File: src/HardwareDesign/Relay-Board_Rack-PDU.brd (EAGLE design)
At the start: 196 x 100 mm, 16 parts

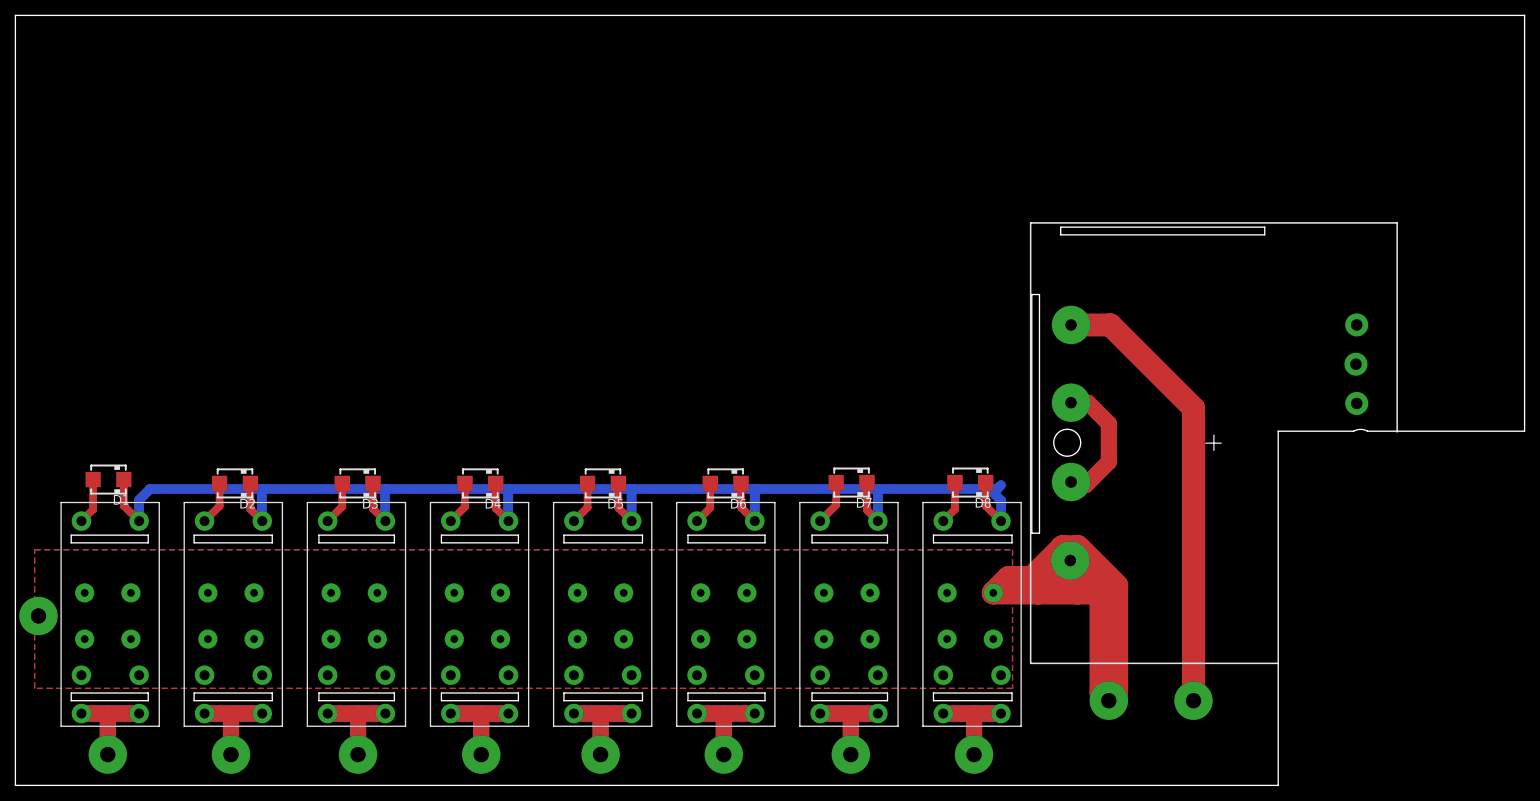
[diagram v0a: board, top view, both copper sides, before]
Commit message: add SMPS to relay board
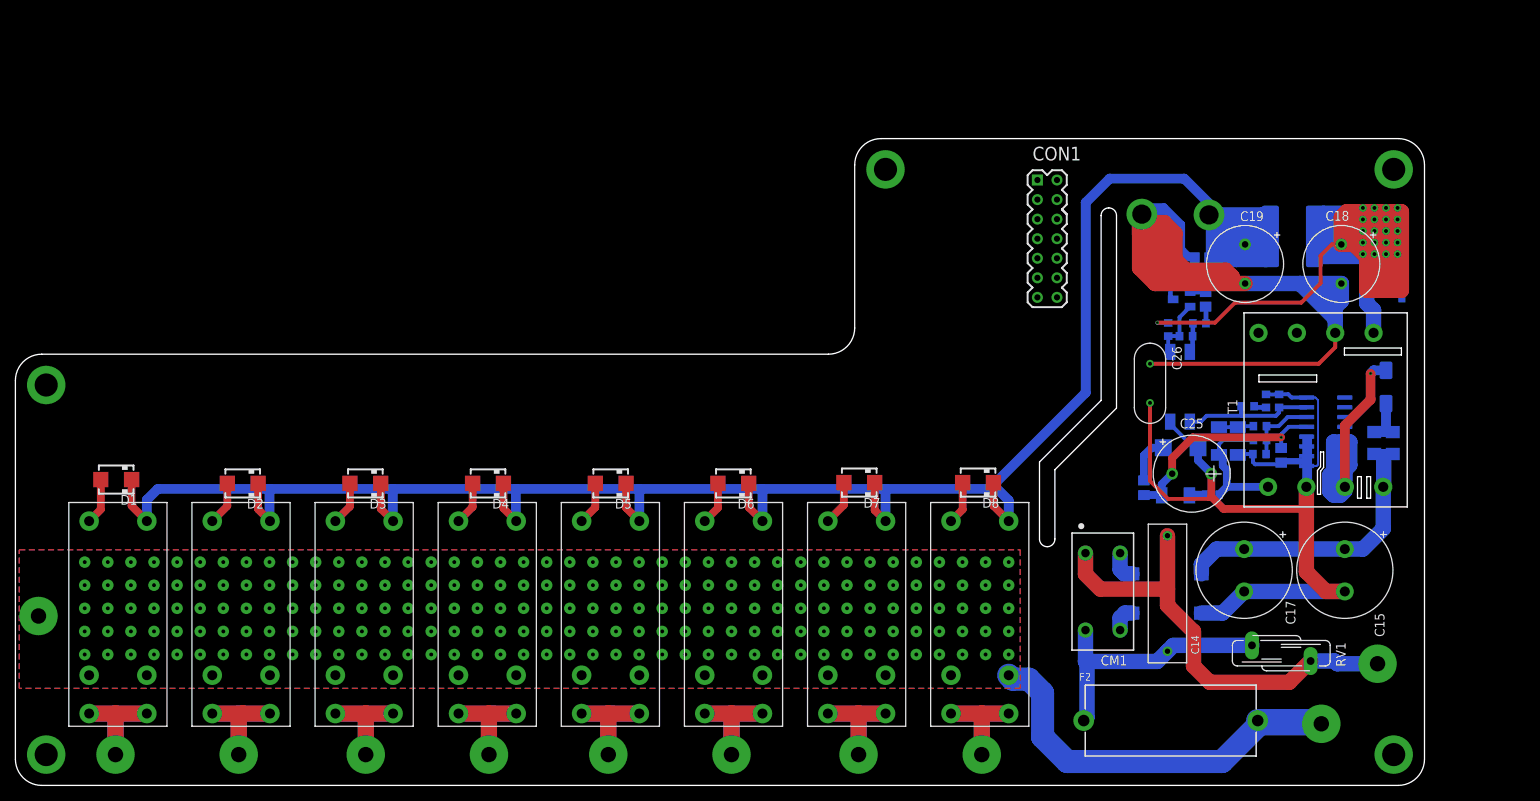
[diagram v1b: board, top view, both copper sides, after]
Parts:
- added BR1: DBLS207G, rectifier:DBS
- added C14: 100nF 275V, ds_passive:103-275V
- added C15, C17: 15uF 400V, Capacitor:CAPPRD550W110D1250H2500B
- added C16: 10nF 1kV, ds_passive:C1206
- added C18: 470uF 25V, Capacitor:CAPPRD508W65D1000H1100B
- added C19, C25: 100uF 25V, Capacitor:CAPPRD508W65D1000H1100B
- added C20: 1uF 25V, ds_passive:C0805
- added C21: 10nF 50V, ds_passive:C0805
- added C22: 2.2nF 50V, ds_passive:C0603
- added C23: 33nF 16V, ds_passive:C0603
- added C24: 220pF, ds_passive:C0805
- added C26: DE2E3KY222MA2BM01, ds_passive:AR21AC103K4R
- added CM1: 20mH CM CHOKE, ds_trafo:WE-CMB_XS_744821120
- added CON1: (no value), ds_con:2X7
- added D15: MRA4007T3G, Diodes:SMA
- added D16: STPS5H100B, ds_active:DPAK_STM
- added D17, D18, D19: BAT41ZFILM, diode:SOD-123_MINI-SMA
- added D20: MMSZ5248B-V-GS08, Diodes-2:DO214AC
- added F2: 696101000002, Wurth_Connectors_WR-FSH:696101000002
- added IC3: TS432ILT, ds_ic_vreg:SOT23
- added IC4: (no value), ds_ic_peripherals:VIPER35HD
- added L2: 3.3uH SD43-332ML, 52101-101-REV-A_v16:INDUCTOR-BOURNS_SRN8040
- added OPT2: SFH6106-2T, ds_ic_peripherals:SMD-4_SFH610X_VIS-M
- added R13: 220K 5% 0.33W 200V, ds_passive:1206
- added R14: 1K, ds_passive:0603
- added R15: 12K, ds_passive:0603
- added R16: 82K, ds_passive:0603
- added R17: 130K 1%, ds_passive:0603
- added R18: 15K 1%, ds_passive:0603
- added R19: 4.7R 1%, ds_passive:0603
- added R20: 330K 1%, ds_passive:0603
- added R21: 133K 1%, ds_passive:0603
- added R22: 30K 1%, ds_passive:0603
- added R23: 47K 1%, ds_passive:0603
- added R24: 220R, ds_passive:0805
- added RV1: B72210S0321K101, varistor:S10K40
- added T1: 750370228, ds_trafo:WE-OLSTM_EE20_L22.2W25H16
- moved D1 1.00 mm to (12.1, 39.7)
- moved D2 1.00 mm to (28.5, 39.2)
- moved D3 1.00 mm to (44.5, 39.2)
- moved D4 1.00 mm to (60.4, 39.2)
- moved D5 1.00 mm to (76.3, 39.2)
- moved D6 1.00 mm to (92.2, 39.2)
- moved D7 1.00 mm to (108.6, 39.3)
- moved D8 1.00 mm to (124.0, 39.3)
- moved REL1 1.00 mm to (12.3, 21.6)
- moved REL2 1.00 mm to (28.2, 21.6)
- moved REL3 1.00 mm to (44.2, 21.6)
- moved REL4 1.00 mm to (60.2, 21.6)
- moved REL5 1.00 mm to (76.2, 21.6)
- moved REL6 1.00 mm to (92.2, 21.6)
- moved REL7 1.00 mm to (108.2, 21.6)
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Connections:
- new net AC_LINE2: C14.2, CM1.1, RV1.2
- new net AGND: BR1.-, C15.2, C17.2, C22.2, C24.2, C25.2, C26.1, D17.A, D20.A, IC4.1, IC4.2, IC4.3, IC4.4, IC4.8, OPT2.4, R22.2, R23.2, T1.3
- new net DC_RAW: BR1.+, C15.1, C16.1, C17.1, R13.2, T1.6
- new net FB: C22.1, C23.1, IC4.7, OPT2.3
- new net GND: C18.2, C19.2, C20.2, C26.2, IC3.3, R18.2, T1.10
- new net N$12: BR1.AC2, CM1.3
- new net N$20: C14.1, CM1.2, F2.2, RV1.1
- new net N$22: C16.2, D15.C, R13.1
- new net N$23: D15.A, IC4.13, IC4.14, IC4.15, IC4.16, T1.4
- new net N$24: D16.2, T1.8
- new net N$25: C18.1, D16.3, L2.1, R14.1
- new net N$26: IC3.2, OPT2.1, R14.2, R15.1
- new net N$27: OPT2.2, R15.2, R16.1
- new net N$28: C21.1, R16.2
- new net N$29: C21.2, IC3.1, R17.2, R18.1
- new net N$30: C24.1, C25.1, D19.C, IC4.5, R24.1
- new net N$31: D19.A, R19.2
- new net N$32: D18.A, R19.1, R20.1, T1.1
- new net N$33: D17.C, D18.C, R21.1
- new net N$34: IC4.6, R20.2, R21.2, R22.1
- new net N$35: C23.2, R23.1
- new net N$36: D20.C, R24.2
- new net N$5: BR1.AC1, CM1.4
- net +12V: now also C19.1, C20.1, L2.2, R17.1
- net AC_LINE: now also F2.1
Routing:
- net GND: track 0.00 -> 193.6 mm, vias 0 -> 1
- net N$25: track 0.00 -> 164.8 mm, vias 0 -> 21
- net AGND: track 0.00 -> 118.3 mm
- net +12V: track 190.9 -> 308.1 mm, vias 0 -> 1
- net N$23: track 0.00 -> 51.0 mm, vias 0 -> 1
- net DC_RAW: track 0.00 -> 38.9 mm
- net N$20: track 0.00 -> 34.4 mm
- net N$30: track 0.00 -> 28.5 mm, vias 0 -> 1
- net AC_LINE: track 81.6 -> 59.0 mm, vias 35 -> 207
- net AC_COM: track 17.7 -> 0.00 mm, vias 2 -> 0
- net FB: track 0.00 -> 17.6 mm
- net N$32: track 0.00 -> 17.4 mm
- net N$34: track 0.00 -> 9.36 mm
- net N$26: track 0.00 -> 8.05 mm
- net N$36: track 0.00 -> 6.18 mm
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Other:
- board size 196 x 100 mm -> 183 x 84 mm

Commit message: finish relay board design
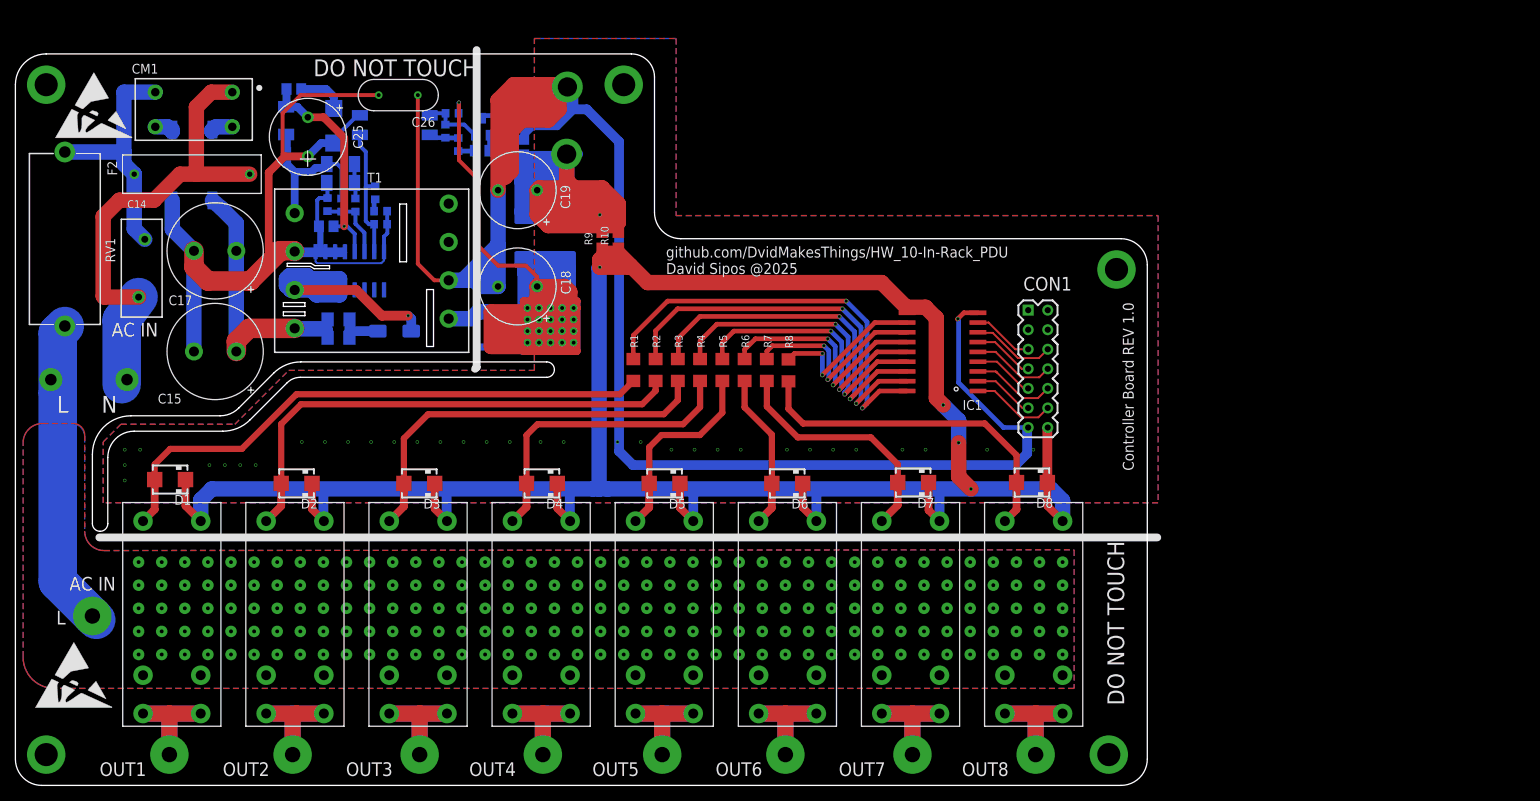
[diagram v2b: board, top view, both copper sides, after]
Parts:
- added IC1: ULN2803, ds_ic_peripherals:SO18
- added R1, R2, R3, R4, R5, R6, R7, R8: 330R 1W, ds_passive:1206
- added R10, R9: 0R, ds_passive:0805
- added U$1, U$2: (no value), logo:ESD_10.00
- BR1: device rectifier:DBS -> ds_active:DIOB_DBLS207G
- RV1: device varistor:S10K40 -> Wurth_EMC Components_WE-VD:WE-VD_10MM_820412001
- moved F2 156.6 mm to (5.42, 71.0), turned to 90 degrees
- moved RV1 156.2 mm to (15.4, 67.2)
- moved C15 149.4 mm to (24.9, 56.4), turned to 180 degrees
- moved C17 139.9 mm to (24.9, 69.4), turned to 180 degrees
- moved BR1 138.2 mm to (22.0, 80.6), turned to 90 degrees
- moved C14 137.9 mm to (21.9, 79.4), turned to 0 degrees
- moved C16 137.6 mm to (41.0, 58.1), turned to 180 degrees
- moved R13 135.5 mm to (41.0, 60.5), turned to 0 degrees
- moved CM1 133.6 mm to (22.2, 87.8), turned to 180 degrees
- moved D15 129.0 mm to (48.2, 59.0), turned to 180 degrees
- moved IC4 128.5 mm to (42.4, 66.8), turned to 270 degrees
- moved R19 127.9 mm to (34.3, 81.5), turned to 90 degrees
- moved C24 127.5 mm to (39.4, 72.6), turned to 0 degrees
- moved D19 125.3 mm to (34.2, 86.3), turned to 270 degrees
- moved R22 125.3 mm to (39.5, 75.4), turned to 90 degrees
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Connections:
- new net +3V3: CON1.1
- new net +5V: CON1.2
- new net I_MEA/TX: CON1.4
- new net N$10: IC1.14, R5.1
- new net N$11: IC1.13, R6.1
- new net N$13: IC1.12, R7.1
- new net N$15: IC1.11, R8.1
- new net N$2: C19.1, C20.1, L2.2, R10.2, R17.1, R9.2
- new net N$6: IC1.18, R1.1
- new net N$7: IC1.17, R2.1
- new net N$8: IC1.16, R3.1
- new net N$9: IC1.15, R4.1
- new net REL_0: CON1.12, IC1.1
- new net REL_1: CON1.11, IC1.2
- new net REL_2: CON1.10, IC1.3
- new net REL_3: CON1.9, IC1.4
- new net REL_4: CON1.8, IC1.5
- new net REL_5: CON1.7, IC1.6
- new net REL_6: CON1.6, IC1.7
- new net REL_7: CON1.5, IC1.8
- new net VMEA/RX: CON1.3
- net +12V: now also CON1.14, IC1.10, R10.1, R9.1; no longer C19.1, C20.1, L2.2, R17.1
- net GND: now also CON1.13, IC1.9
- net RELAY_1: now also R1.2
- net RELAY_2: now also R2.2
- net RELAY_3: now also R3.2
- net RELAY_4: now also R4.2
- net RELAY_5: now also R5.2
- net RELAY_6: now also R6.2
- net RELAY_7: now also R7.2
- net RELAY_8: now also R8.2
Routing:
- net GND: track 193.6 -> 321.8 mm, vias 1 -> 38
- net N$2: track 0.00 -> 126.7 mm, vias 1 -> 2
- net +12V: track 308.1 -> 411.9 mm, vias 1 -> 4
- net RELAY_1: track 6.02 -> 74.6 mm
- net RELAY_2: track 5.70 -> 65.1 mm
- net N$25: track 164.8 -> 221.5 mm
- net N$6: track 0.00 -> 54.6 mm, vias 1 -> 2
- net N$7: track 0.00 -> 50.5 mm, vias 0 -> 2
- net RELAY_3: track 5.68 -> 52.8 mm
- net N$8: track 0.00 -> 45.5 mm, vias 0 -> 2
- net N$9: track 0.00 -> 40.6 mm, vias 0 -> 2
- net RELAY_8: track 5.63 -> 44.9 mm
- net N$10: track 0.00 -> 36.0 mm, vias 0 -> 2
- net RELAY_4: track 5.65 -> 39.4 mm
- net N$11: track 0.00 -> 31.0 mm, vias 0 -> 2
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- added copper zone on layer 1, net GND
- added copper zone on layer 16, net GND
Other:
- board size 183 x 84 mm -> 147 x 95 mm
- board text added: "AC IN"
- board text added: "Controller Board REV 1.0"
- board text added: "DO NOT TOUCH"
- board text added: "L"
- board text added: "L N"
- board text added: "OUT1"
- board text added: "OUT2"
- board text added: "OUT3"
- board text added: "OUT4"
- board text added: "OUT5"
- board text added: "OUT6"
- board text added: "OUT7"
- board text added: "OUT8"
- board text added: "github.com/DvidMakesThings/HW_10-In-Rack_PDU David Sipos @2025"
